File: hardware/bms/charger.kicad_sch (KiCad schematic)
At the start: 36 parts

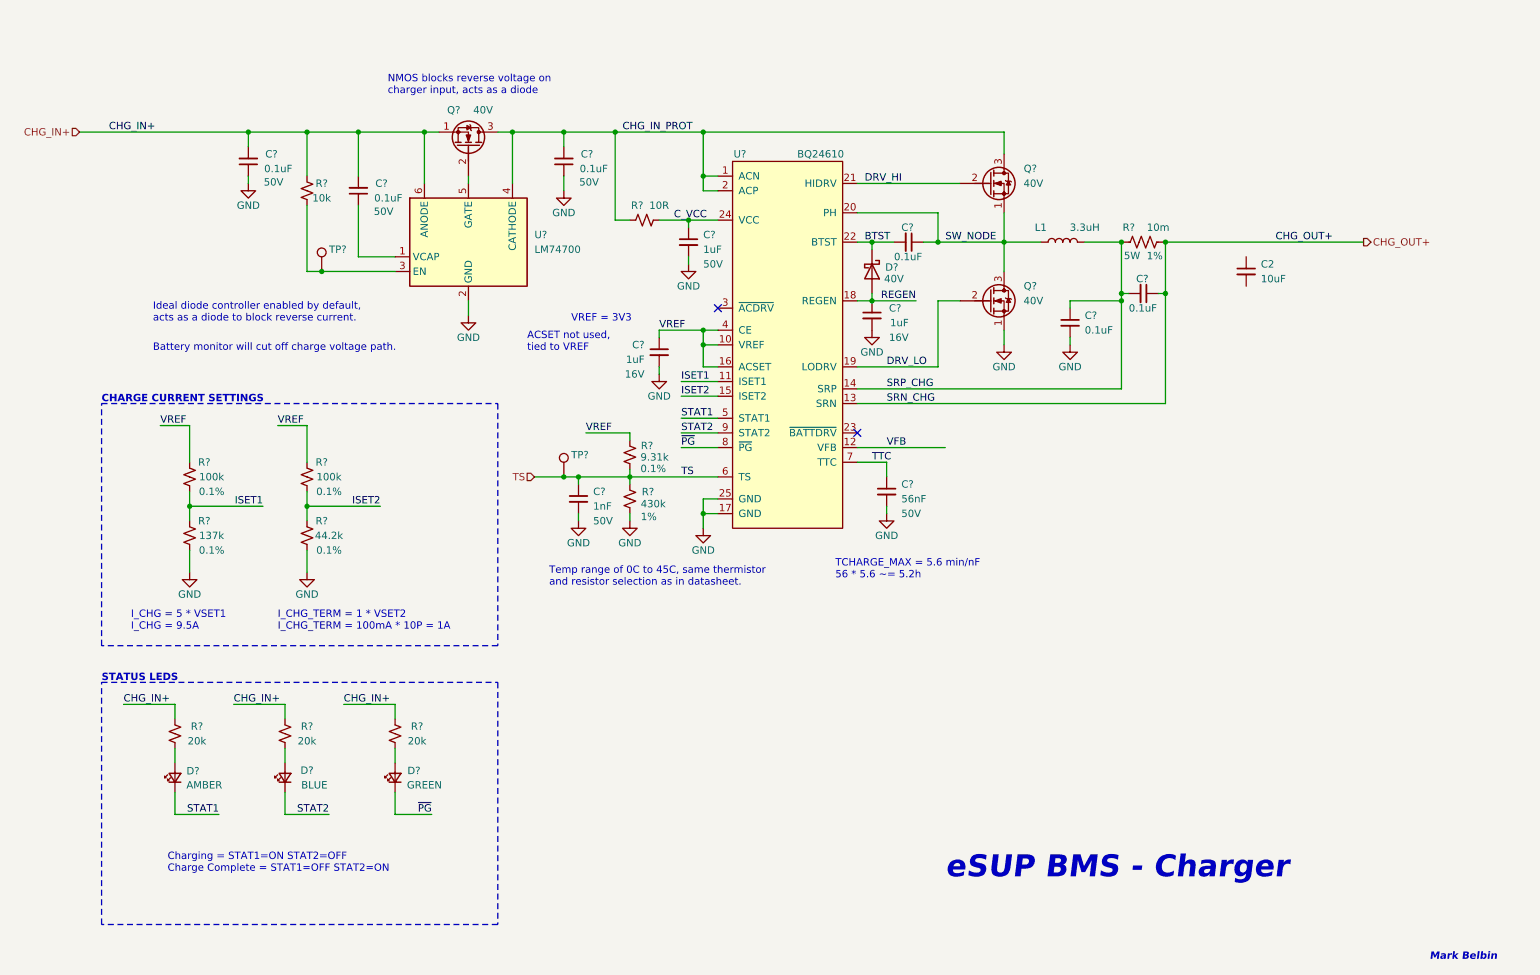
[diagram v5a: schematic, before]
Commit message: Charger schematic complete! Only MCU left.
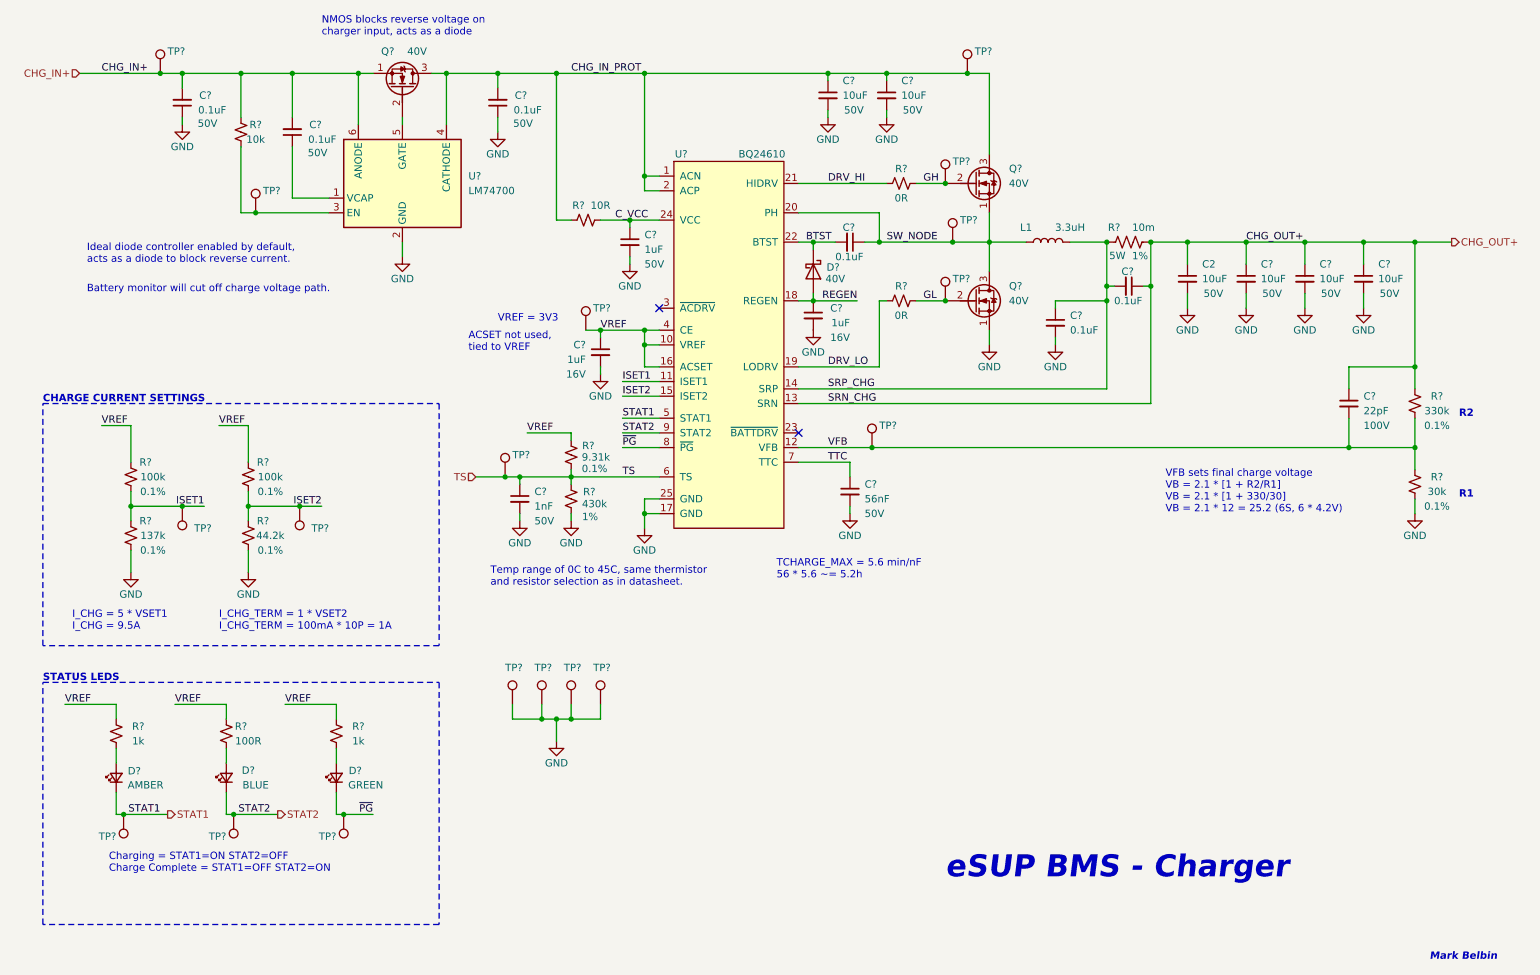
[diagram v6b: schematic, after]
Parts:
- removed R? (x2): 20k, Resistor_SMD:R_0603_1608Metric, symbol Device:R_Small_US
- added C?: 22pF, Capacitor_SMD:C_0603_1608Metric, symbol Device:C_Small
- added C? (x5): 10uF, Capacitor_SMD:C_1210_3225Metric, symbol Device:C_Small
- added R?: 100R, Resistor_SMD:R_0603_1608Metric, symbol Device:R_Small_US
- added R?: 1k, Resistor_SMD:R_0603_1608Metric, symbol Device:R_Small_US
- added R? (x2): 0R, Resistor_SMD:R_0603_1608Metric, symbol Device:R_Small_US
- added R?: 30k, Resistor_SMD:R_0603_1608Metric, symbol Device:R_Small_US
- added R?: 330k, Resistor_SMD:R_0603_1608Metric, symbol Device:R_Small_US
- added TP? (x16): TestPoint, TestPoint:TestPoint_Pad_D1.0mm, symbol Connector:TestPoint
- C2: footprint (none) -> Capacitor_SMD:C_1210_3225Metric; MFG (none) -> Murata Electronics; MFG PN (none) -> GCM32EC71H106KA03K; Voltage (none) -> 50V
- L1: footprint (none) -> bms:HCM1307-3R3-R; DCR (none) -> 4.5m; Imax (none) -> 15A; MFG (none) -> Eaton - Electronics Division; MFG PN (none) -> HCM1307-3R3-R
- R?: value 20k -> 1k; MFG PN ERJ-3EKF2002V -> ERJ-3EKF1001V; Power (none) -> 1/10W
- R?: MFG Vishay Dale -> KOA Speer Electronics, Inc.; MFG PN (none) -> TLRH3APTTE10L0F
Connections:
- net CHG_IN+: now also TP?.1; no longer R?.2
- net CHG_IN_PROT: now also C?.1, C?.1, TP?.1
- net CHG_OUT+: now also C2.1, C?.1, C?.1, C?.1, C?.1, R?.2
- net DRV_HI: now also R?.1; no longer Q?.2 (G)
- net DRV_LO: now also R?.1; no longer Q?.2 (G)
- net GND: now also C2.2, C?.2, C?.2, C?.2, C?.2, C?.2, R?.1, TP?.1, TP?.1, TP?.1, TP?.1
- net ISET1: now also TP?.1
- net ISET2: now also TP?.1
- net STAT1: now also TP?.1
- net STAT2: now also TP?.1
- net SW_NODE: now also TP?.1
- net VFB: now also C?.2, R?.1, R?.2, TP?.1
- net VREF: now also R?.2, R?.2, R?.2, TP?.1
- net ~{PG}: now also TP?.1
- net at D?.2 (A): now also R?.1 (x2)
- new net GH: Q?.2 (G), R?.2, TP?.1
- new net GL: Q?.2 (G), R?.2, TP?.1
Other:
- note added: "R1"
- note added: "R2"
- note added: "VFB sets final charge voltage VB = 2.1 * [1 + R2/R1] VB = 2.1 * [1 + 330/30] VB = 2.1 * 12 = 25.2 (6S, 6 * 4.2V)"
- moved on the sheet: C2, C?, D?, L1, Q?, R?, TP?, U?

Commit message: Choose MCU as ESP32-C3-MINI. Small form factor with just enough I/O.
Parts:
- added TP? (x2): TestPoint, TestPoint:TestPoint_Pad_D1.0mm, symbol Connector:TestPoint
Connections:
- net REGEN: now also TP?.1
- net DG: now reaches Q?.2 (G), U?.5 (GATE)
- net DG: now also TP?.1
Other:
- moved on the sheet: R?
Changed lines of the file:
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@@
 (kicad_sch (version 20230121) (generator eeschema)
   (paper "A4")
+  (title_block
+    (date "2023-10-25")
+  )
   (junction (at 182.88 66.04) (diameter 0) (color 0 0 0 0)
   )
@@
   (junction (at 129.54 81.28) (diameter 0) (color 0 0 0 0)
   )
+  (junction (at 87.63 45.72) (diameter 0) (color 0 0 0 0)
+  )
   (junction (at 104.14 36.83) (diameter 0) (color 0 0 0 0)
   )
@@
     (stroke (width 0) (type default))
   )
-  (wire (pts (xy 158.75 76.2) (xy 166.37 76.2))
+  (wire (pts (xy 158.75 76.2) (xy 167.64 76.2))
     (stroke (width 0) (type default))
   )
@@
     (stroke (width 0) (type default))
   )
-  (wire (pts (xy 156.21 87.63) (xy 170.18 87.63))
+  (wire (pts (xy 156.21 87.63) (xy 171.45 87.63))
     (stroke (width 0) (type default))
   )
@@
     (stroke (width 0) (type default))
   )
-  (wire (pts (xy 176.53 55.88) (xy 181.61 55.88))
+  (wire (pts (xy 177.8 55.88) (xy 181.61 55.88))
     (stroke (width 0) (type default))
   )
@@
     (stroke (width 0) (type default))
   )
+  (wire (pts (xy 82.55 45.72) (xy 87.63 45.72))
+    (stroke (width 0) (type default))
+  )
   (wire (pts (xy 76.2 146.05) (xy 76.2 148.59))
     (stroke (width 0) (type default))
@@
     (stroke (width 0) (type default))
   )
-  (wire (pts (xy 170.18 87.63) (xy 170.18 76.2))
+  (wire (pts (xy 171.45 87.63) (xy 171.45 76.2))
     (stroke (width 0) (type default))
   )
@@
     (stroke (width 0) (type default))
   )
-  (wire (pts (xy 156.21 55.88) (xy 171.45 55.88))
+  (wire (pts (xy 156.21 55.88) (xy 172.72 55.88))
     (stroke (width 0) (type default))
   )
@@
     (stroke (width 0) (type default))
   )
-  (wire (pts (xy 176.53 76.2) (xy 181.61 76.2))
+  (wire (pts (xy 177.8 76.2) (xy 181.61 76.2))
     (stroke (width 0) (type default))
   )
@@
     (stroke (width 0) (type default))
   )
-  (wire (pts (xy 170.18 76.2) (xy 171.45 76.2))
+  (wire (pts (xy 171.45 76.2) (xy 172.72 76.2))
     (stroke (width 0) (type default))
   )
@@
     (effects (font (size 1.27 1.27)) (justify left bottom))
   )
+  (label "DG" (at 83.82 45.72 0) (fields_autoplaced)
+    (effects (font (size 1.27 1.27)) (justify left bottom))
+  )
   (label "ISET1" (at 53.34 111.76 180) (fields_autoplaced)
     (effects (font (size 1.27 1.27)) (justify right bottom))
@@
     )
   )
-  (symbol (lib_id "Device:R_Small_US") (at 173.99 55.88 90) (unit 1)
+  (symbol (lib_id "Device:R_Small_US") (at 175.26 55.88 90) (unit 1)
     (in_bom yes) (on_board yes) (dnp no)
-    (property "Reference" "R?" (at 173.99 53.34 90)
+    (property "Reference" "R?" (at 175.26 53.34 90)
       (effects (font (size 1.27 1.27)))
     )
-    (property "Value" "0R" (at 173.99 58.42 90)
+    (property "Value" "0R" (at 175.26 58.42 90)
       (effects (font (size 1.27 1.27)))
     )
-    (property "Footprint" "Resistor_SMD:R_0603_1608Metric" (at 173.99 55.88 0)
+    (property "Footprint" "Resistor_SMD:R_0603_1608Metric" (at 175.26 55.88 0)
       (effects (font (size 1.27 1.27)) hide)
     )
-    (property "Datasheet" "~" (at 173.99 55.88 0)
+    (property "Datasheet" "~" (at 175.26 55.88 0)
       (effects (font (size 1.27 1.27)) hide)
     )
-    (property "MFG" "Panasonic Electronic Components" (at 173.99 55.88 90)
+    (property "MFG" "Panasonic Electronic Components" (at 175.26 55.88 90)
       (effects (font (size 1.27 1.27)) hide)
     )
-    (property "MFG PN" "ERJ-3GEY0R00V" (at 173.99 55.88 90)
+    (property "MFG PN" "ERJ-3GEY0R00V" (at 175.26 55.88 90)
       (effects (font (size 1.27 1.27)) hide)
     )
@@
     )
   )
-  (symbol (lib_id "Device:R_Small_US") (at 173.99 76.2 90) (unit 1)
+  (symbol (lib_id "Device:R_Small_US") (at 175.26 76.2 90) (unit 1)
     (in_bom yes) (on_board yes) (dnp no)
-    (property "Reference" "R?" (at 173.99 73.66 90)
+    (property "Reference" "R?" (at 175.26 73.66 90)
       (effects (font (size 1.27 1.27)))
     )
-    (property "Value" "0R" (at 173.99 78.74 90)
+    (property "Value" "0R" (at 175.26 78.74 90)
       (effects (font (size 1.27 1.27)))
     )
-    (property "Footprint" "Resistor_SMD:R_0603_1608Metric" (at 173.99 76.2 0)
+    (property "Footprint" "Resistor_SMD:R_0603_1608Metric" (at 175.26 76.2 0)
       (effects (font (size 1.27 1.27)) hide)
     )
-    (property "Datasheet" "~" (at 173.99 76.2 0)
+    (property "Datasheet" "~" (at 175.26 76.2 0)
       (effects (font (size 1.27 1.27)) hide)
     )
-    (property "MFG" "Panasonic Electronic Components" (at 173.99 76.2 90)
+    (property "MFG" "Panasonic Electronic Components" (at 175.26 76.2 90)
       (effects (font (size 1.27 1.27)) hide)
     )
-    (property "MFG PN" "ERJ-3GEY0R00V" (at 173.99 76.2 90)
+    (property "MFG PN" "ERJ-3GEY0R00V" (at 175.26 76.2 90)
       (effects (font (size 1.27 1.27)) hide)
     )
@@
     )
   )
+  (symbol (lib_id "Connector:TestPoint") (at 167.64 76.2 0) (unit 1)
+    (in_bom yes) (on_board yes) (dnp no)
+    (property "Reference" "TP?" (at 168.91 72.39 0)
+      (effects (font (size 1.27 1.27)) (justify left))
+    )
+    (property "Value" "TestPoint" (at 169.1132 75.5142 0)
+      (effects (font (size 1.27 1.27)) (justify left) hide)
+    )
+    (property "Footprint" "TestPoint:TestPoint_Pad_D1.0mm" (at 172.72 76.2 0)
+      (effects (font (size 1.27 1.27)) hide)
+    )
+    (property "Datasheet" "~" (at 172.72 76.2 0)
+      (effects (font (size 1.27 1.27)) hide)
+    )
+    (pin "1")
+    (instances
+      (project "bms"
+        (path "/a4805e9d-b940-444e-a7cb-db4f4c53ed46/00000000-0000-0000-0000-00006523a805"
+          (reference "TP?") (unit 1)
+        )
+        (path "/a4805e9d-b940-444e-a7cb-db4f4c53ed46/00000000-0000-0000-0000-00006523ab32"
+          (reference "TP?") (unit 1)
+        )
+      )
+    )
+  )
   (symbol (lib_id "Device:D_Schottky") (at 158.75 71.12 270) (unit 1)
     (in_bom yes) (on_board yes) (dnp no)
@@
       (effects (font (size 1.27 1.27)) hide)
     )
+    (pin "1")
+    (instances
+      (project "bms"
+        (path "/a4805e9d-b940-444e-a7cb-db4f4c53ed46/00000000-0000-0000-0000-00006523a805"
+          (reference "TP?") (unit 1)
+        )
+        (path "/a4805e9d-b940-444e-a7cb-db4f4c53ed46/00000000-0000-0000-0000-00006523ab32"
+          (reference "TP?") (unit 1)
+        )
+      )
+    )
+  )
+  (symbol (lib_id "Connector:TestPoint") (at 82.55 45.72 0) (unit 1)
+    (in_bom yes) (on_board yes) (dnp no)
+    (property "Reference" "TP?" (at 83.82 41.91 0)
+      (effects (font (size 1.27 1.27)) (justify left))
+    )
+    (property "Value" "TestPoint" (at 84.0232 45.0342 0)
+      (effects (font (size 1.27 1.27)) (justify left) hide)
+    )
+    (property "Footprint" "TestPoint:TestPoint_Pad_D1.0mm" (at 87.63 45.72 0)
+      (effects (font (size 1.27 1.27)) hide)
+    )
+    (property "Datasheet" "~" (at 87.63 45.72 0)
+      (effects (font (size 1.27 1.27)) hide)
+    )

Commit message: MCU power conversion section complete
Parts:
- added D?: BLUE, LED_SMD:LED_0603_1608Metric, symbol Device:LED_Small
- added R?: 10k, Resistor_SMD:R_0603_1608Metric, symbol Device:R_Small_US
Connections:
- net CHG_IN+: now also R?.1
- net GND: now also D?.1 (K)
- new net: D?.2 (A), R?.2
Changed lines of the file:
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@@
   (junction (at 129.54 83.82) (diameter 0) (color 0 0 0 0)
   )
+  (junction (at 34.29 36.83) (diameter 0) (color 0 0 0 0)
+  )
   (junction (at 170.18 66.04) (diameter 0) (color 0 0 0 0)
   )
@@
     (stroke (width 0) (type default))
   )
+  (wire (pts (xy 34.29 36.83) (xy 34.29 39.37))
+    (stroke (width 0) (type default))
+  )
   (wire (pts (xy 209.55 73.66) (xy 210.82 73.66))
     (stroke (width 0) (type default))
@@
     (stroke (width 0) (type default))
   )
+  (wire (pts (xy 34.29 52.07) (xy 34.29 53.34))
+    (stroke (width 0) (type default))
+  )
   (wire (pts (xy 49.53 36.83) (xy 59.69 36.83))
     (stroke (width 0) (type default))
@@
     (stroke (width 0) (type default))
   )
+  (wire (pts (xy 34.29 36.83) (xy 45.72 36.83))
+    (stroke (width 0) (type default))
+  )
   (wire (pts (xy 107.95 106.68) (xy 116.84 106.68))
     (stroke (width 0) (type default))
@@
     (stroke (width 0) (type default))
   )
+  (wire (pts (xy 34.29 44.45) (xy 34.29 46.99))
+    (stroke (width 0) (type default))
+  )
   (wire (pts (xy 262.89 66.04) (xy 262.89 87.63))
     (stroke (width 0) (type default))
@@
     (stroke (width 0) (type default))
   )
-  (wire (pts (xy 31.75 36.83) (xy 45.72 36.83))
+  (wire (pts (xy 31.75 36.83) (xy 34.29 36.83))
     (stroke (width 0) (type default))
   )
@@
     )
   )
+  (symbol (lib_id "power:GND") (at 34.29 53.34 0) (unit 1)
+    (in_bom yes) (on_board yes) (dnp no)
+    (property "Reference" "#PWR048" (at 34.29 59.69 0)
+      (effects (font (size 1.27 1.27)) hide)
+    )
+    (property "Value" "GND" (at 34.29 57.15 0)
+      (effects (font (size 1.27 1.27)))
+    )
+    (property "Footprint" "" (at 34.29 53.34 0)
+      (effects (font (size 1.27 1.27)) hide)
+    )
+    (property "Datasheet" "" (at 34.29 53.34 0)
+      (effects (font (size 1.27 1.27)) hide)
+    )
+    (pin "1")
+    (instances
+      (project "bms"
+        (path "/a4805e9d-b940-444e-a7cb-db4f4c53ed46"
+          (reference "#PWR048") (unit 1)
+        )
+        (path "/a4805e9d-b940-444e-a7cb-db4f4c53ed46/00000000-0000-0000-0000-00006523ab32"
+          (reference "#PWR048") (unit 1)
+        )
+      )
+    )
+  )
   (symbol (lib_id "Connector:TestPoint") (at 106.68 146.05 0) (unit 1)
     (in_bom yes) (on_board yes) (dnp no)
@@
     )
   )
+  (symbol (lib_id "Device:LED_Small") (at 34.29 49.53 90) (unit 1)
+    (in_bom yes) (on_board yes) (dnp no)
+    (property "Reference" "D?" (at 38.1 48.26 90)
+      (effects (font (size 1.27 1.27)))
+    )
+    (property "Value" "BLUE" (at 39.37 50.8 90)
+      (effects (font (size 1.27 1.27)) hide)
+    )
+    (property "Footprint" "LED_SMD:LED_0603_1608Metric" (at 34.29 49.53 90)
+      (effects (font (size 1.27 1.27)) hide)
+    )
+    (property "Datasheet" "~" (at 34.29 49.53 90)
+      (effects (font (size 1.27 1.27)) hide)
+    )
+    (property "MFG" "Würth Elektronik" (at 34.29 49.53 90)
+      (effects (font (size 1.27 1.27)) hide)
+    )
+    (property "MFG PN" "150060BS75000" (at 34.29 49.53 90)
+      (effects (font (size 1.27 1.27)) hide)
+    )
+    (property "VF" "3.2V" (at 34.29 49.53 90)
+      (effects (font (size 1.27 1.27)) hide)
+    )
+    (pin "1")
+    (pin "2")
+    (instances
+      (project "bms"
+        (path "/a4805e9d-b940-444e-a7cb-db4f4c53ed46/00000000-0000-0000-0000-00006523ab32"
+          (reference "D?") (unit 1)
+        )
+        (path "/a4805e9d-b940-444e-a7cb-db4f4c53ed46"
+          (reference "D?") (unit 1)
+        )
+      )
+    )
+  )
   (symbol (lib_id "Device:C_Small") (at 107.95 110.49 0) (unit 1)
     (in_bom yes) (on_board yes) (dnp no)
@@
         )
       )
+    )
+  )
+  (symbol (lib_id "Device:R_Small_US") (at 34.29 41.91 0) (unit 1)
+    (in_bom yes) (on_board yes) (dnp no)
+    (property "Reference" "R?" (at 37.5654 40.2469 0)
+      (effects (font (size 1.27 1.27)))
+    )
+    (property "Value" "10k" (at 38.0057 42.1056 0)
+      (effects (font (size 1.27 1.27)))
+    )
+    (property "Footprint" "Resistor_SMD:R_0603_1608Metric" (at 34.29 41.91 0)
+      (effects (font (size 1.27 1.27)) hide)
+    )
+    (property "Datasheet" "~" (at 34.29 41.91 0)
+      (effects (font (size 1.27 1.27)) hide)
+    )
+    (property "MFG" "Panasonic Electronic Components" (at 34.29 41.91 90)
+      (effects (font (size 1.27 1.27)) hide)
+    )
+    (property "MFG PN" "ERJ-UP3F1002V" (at 34.29 41.91 90)
+      (effects (font (size 1.27 1.27)) hide)
+    )
+    (property "Power" "1/4W" (at 38.8861 44.2089 0)
+      (effects (font (size 1.27 1.27)))
+    )
+    (pin "1")
+    (pin "2")
+    (instances
+      (project "bms"
+        (path "/a4805e9d-b940-444e-a7cb-db4f4c53ed46/00000000-0000-0000-0000-00006523a805"
+          (reference "R?") (unit 1)
+        )
+        (path "/a4805e9d-b940-444e-a7cb-db4f4c53ed46"
+          (reference "R?") (unit 1)
+        )
+        (path "/a4805e9d-b940-444e-a7cb-db4f4c53ed46/00000000-0000-0000-0000-00006523ab32"
+          (reference "R?") (unit 1)
+        )
+      )
